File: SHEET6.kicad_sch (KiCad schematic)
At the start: 30 parts, among them U12 74LS245, U27 74LS02, U37 RAM_64K_X_1, U38 RAM_64K_X_1, U39 RAM_64K_X_1, U40 RAM_64K_X_1, U41 RAM_64K_X_1, U42 RAM_64K_X_1, U43 RAM_64K_X_1, U44 RAM_64K_X_1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

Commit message: Fixed LS and S parts
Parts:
- U94: value 74LS280 -> 74S280
- U97: value 74LS08 -> 74S08
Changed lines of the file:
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@@
 			)
 		)
-		(property "Value" "74LS280"
+		(property "Value" "74S280"
 			(at 180.34 125.73 0)
 			(effects
@@
 			)
 		)
-		(property "Value" "74LS08"
+		(property "Value" "74S08"
 			(at 102.87 107.95 0)
 			(effects

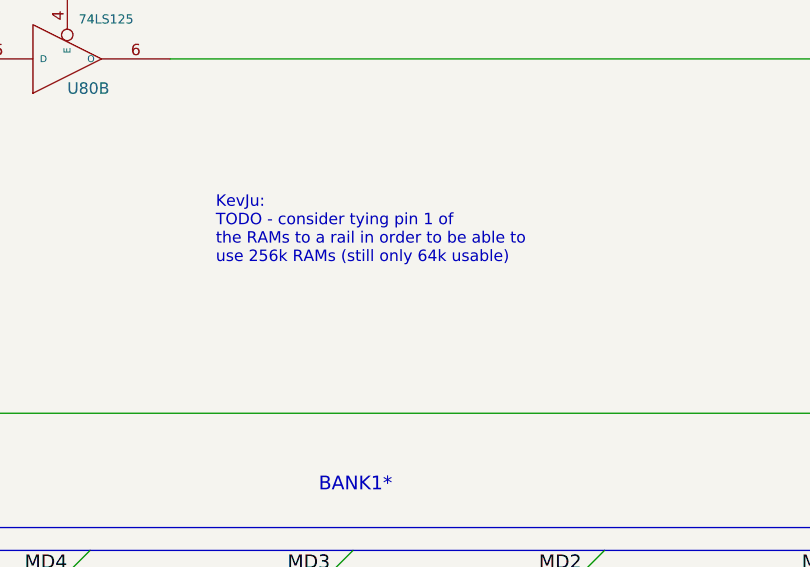
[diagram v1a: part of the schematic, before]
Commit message: added BOM
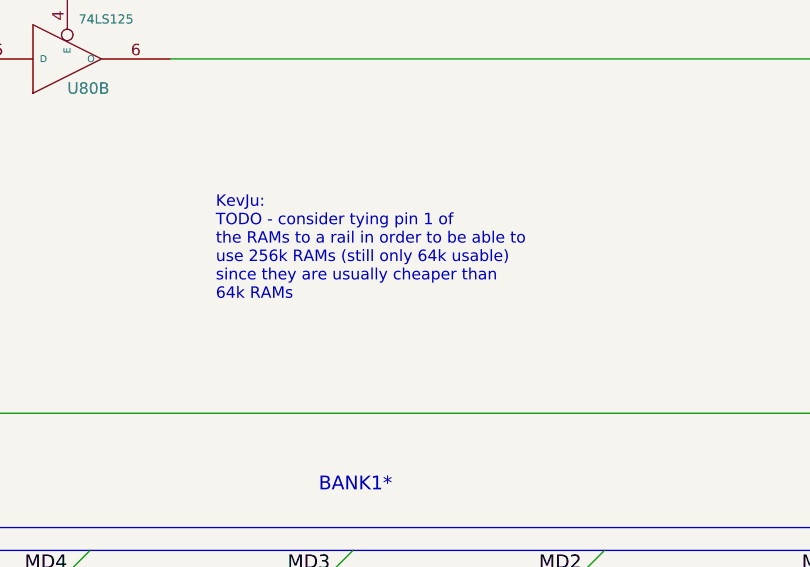
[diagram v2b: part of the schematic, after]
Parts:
- R23: Link (none) -> https://www.digikey.com/en/products/detail/yageo/MFR-25FTE5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
- RN4: Link (none) -> https://www.digikey.com/en/products/detail/bourns-inc/4116R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; Note (none) -> 33 Ohm will work fine here
- U12, U27, U62, U79, U80, U83, U96, U97, U99: Link (none) -> https://www.digikey.com/en/products/detail/texas-instrument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
- U37, U38, U39, U40, U41, U42, U43, U44, U45, U53, U54, U55, U56, U57, U58, U59, U60, U61: Link (none) -> https://www.jameco.com/z/KM4164B-12-Samsung-Electronics-IC-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
- U94: Link (none) -> https://www.jameco.com/z/DM74S280N-National-Semiconductor-9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; Note (none) -> *** Investigate replacing this
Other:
- note added: "KevJu: TODO - consider tying pin 1 of the RAMs to a rail in order to be able to use 256k RAMs (still only 64k usable) since they are usually cheaper than 64k RAMs"
- note removed: "KevJu: TODO - consider tying pin 1 of the RAMs to a rail in order to be able to use 256k RAMs (still only 64k usable)"
